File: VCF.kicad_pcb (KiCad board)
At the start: 2 copper layers, 70 x 70 mm, 41 parts, among them J1 Conn_01x05_Male, J10 Conn_01x05_Male, J11 Input, J12 Conn_01x05_Male, J2 Conn_01x05_Male, J3 Env, J4 Conn_01x05_Male, J5 Conn_01x05_Male, J6 Conn_01x05_Male, J7 Conn_01x05_Male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

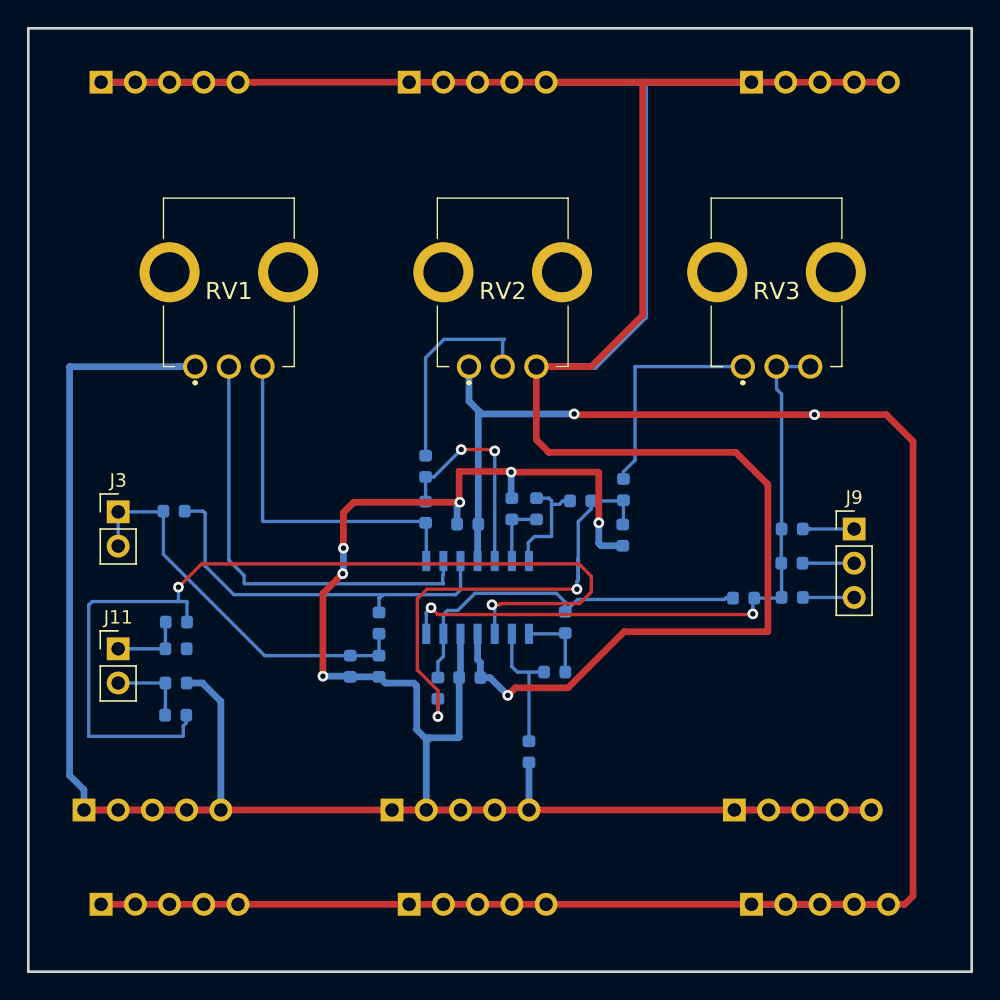
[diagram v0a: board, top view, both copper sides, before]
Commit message: Плата 40х70 мм. Добавленны подписи компонентов и регуляторов Косметические изменения в схеме, уменьшенно количество разъемов питания
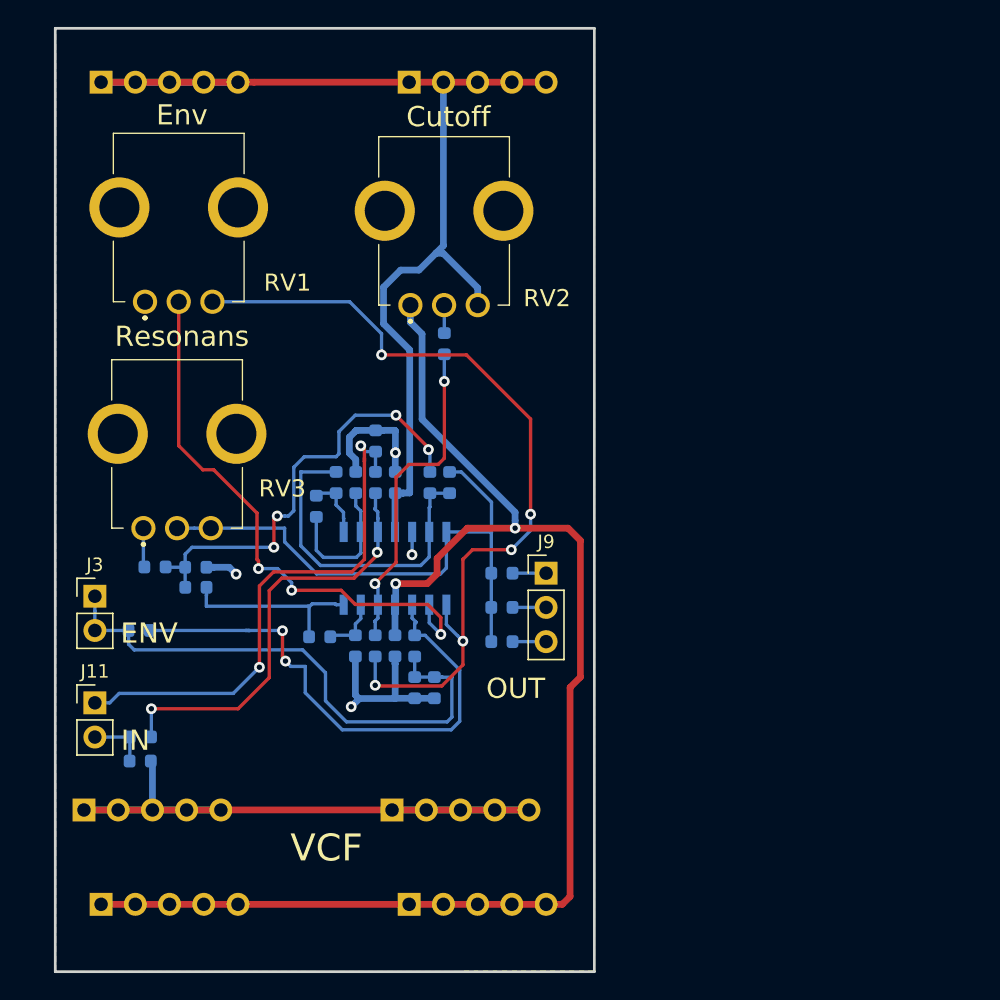
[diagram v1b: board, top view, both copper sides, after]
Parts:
- removed J2, J5, J8: Conn_01x05_Male, footprint:pls1x05
- moved RV3 46.1 mm to (31.0, 51.5)
- moved C4 35.2 mm to (29.4, 60.0), turned to 0 degrees
- moved D1 31.8 mm to (32.4, 60.0), turned to 180 degrees
- moved R4 29.3 mm to (32.4, 61.5), turned to 0 degrees
- moved R10 23.8 mm to (44.3, 53.7), turned to 90 degrees
- moved R13 23.4 mm to (51.3, 53.7), turned to 270 degrees
- moved J9 23.1 mm to (58.4, 60.4)
- moved R12 21.8 mm to (55.1, 60.4)
- moved R17 21.8 mm to (55.1, 65.5)
- moved R14 21.8 mm to (55.1, 63.0)
- moved R11 21.5 mm to (41.4, 55.5), turned to 270 degrees
- moved R19 21.4 mm to (45.8, 50.6), turned to 90 degrees
- moved R15 19.9 mm to (42.8, 53.7)
- moved R2 18.7 mm to (41.6, 65.2), turned to 0 degrees
- moved R16 18.0 mm to (45.8, 53.7), turned to 90 degrees
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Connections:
- net GNDREF renamed GND
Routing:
- net GND: track 218.7 -> 83.4 mm, vias 6 -> 4
- net -5V: track 199.6 -> 86.5 mm, vias 1 -> 0
- net +5V: track 152.3 -> 101.9 mm
- net Net-(R16-Pad1): track 71.3 -> 32.1 mm
- net Net-(R6-Pad2): track 26.2 -> 62.7 mm, vias 0 -> 5
- net Net-(J11-Pad1): track 5.50 -> 39.6 mm, vias 0 -> 2
- net Net-(C4-Pad1): track 16.7 -> 2.93 mm
- net Net-(R9-Pad2): track 15.7 -> 2.08 mm
- net /ENV_2: track 29.9 -> 41.0 mm
- net Net-(R3-Pad1): track 29.2 -> 39.6 mm, vias 0 -> 2
- net Net-(RV1-Pad2): track 33.1 -> 41.9 mm, vias 0 -> 3
- net Net-(R6-Pad1): track 16.0 -> 24.4 mm
- net Net-(R12-Pad2): track 49.8 -> 42.6 mm, vias 2 -> 0
- net Net-(R2-Pad1): track 8.62 -> 14.0 mm
- net Net-(C3-Pad2): track 28.4 -> 24.7 mm
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- added copper zone on B.Cu, net GND
- added copper zone on F.Cu, net GND
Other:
- board size 70 x 70 mm -> 40 x 70 mm
- board text added: "Cutoff"
- board text added: "ENV"
- board text added: "Env"
- board text added: "IN"
- board text added: "OUT"
- board text added: "Resonans"
- board text added: "VCF"
